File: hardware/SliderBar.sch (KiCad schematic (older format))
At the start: 36 parts, among them J1 USB_B_Mini, J2 MOTOR_OUT, J3 POT_IN, J4 DEBUG, U1 MIC5205-3.3YM5, U2 MT3608, U3 STM32F072C8Tx, U4 TB6612FNG

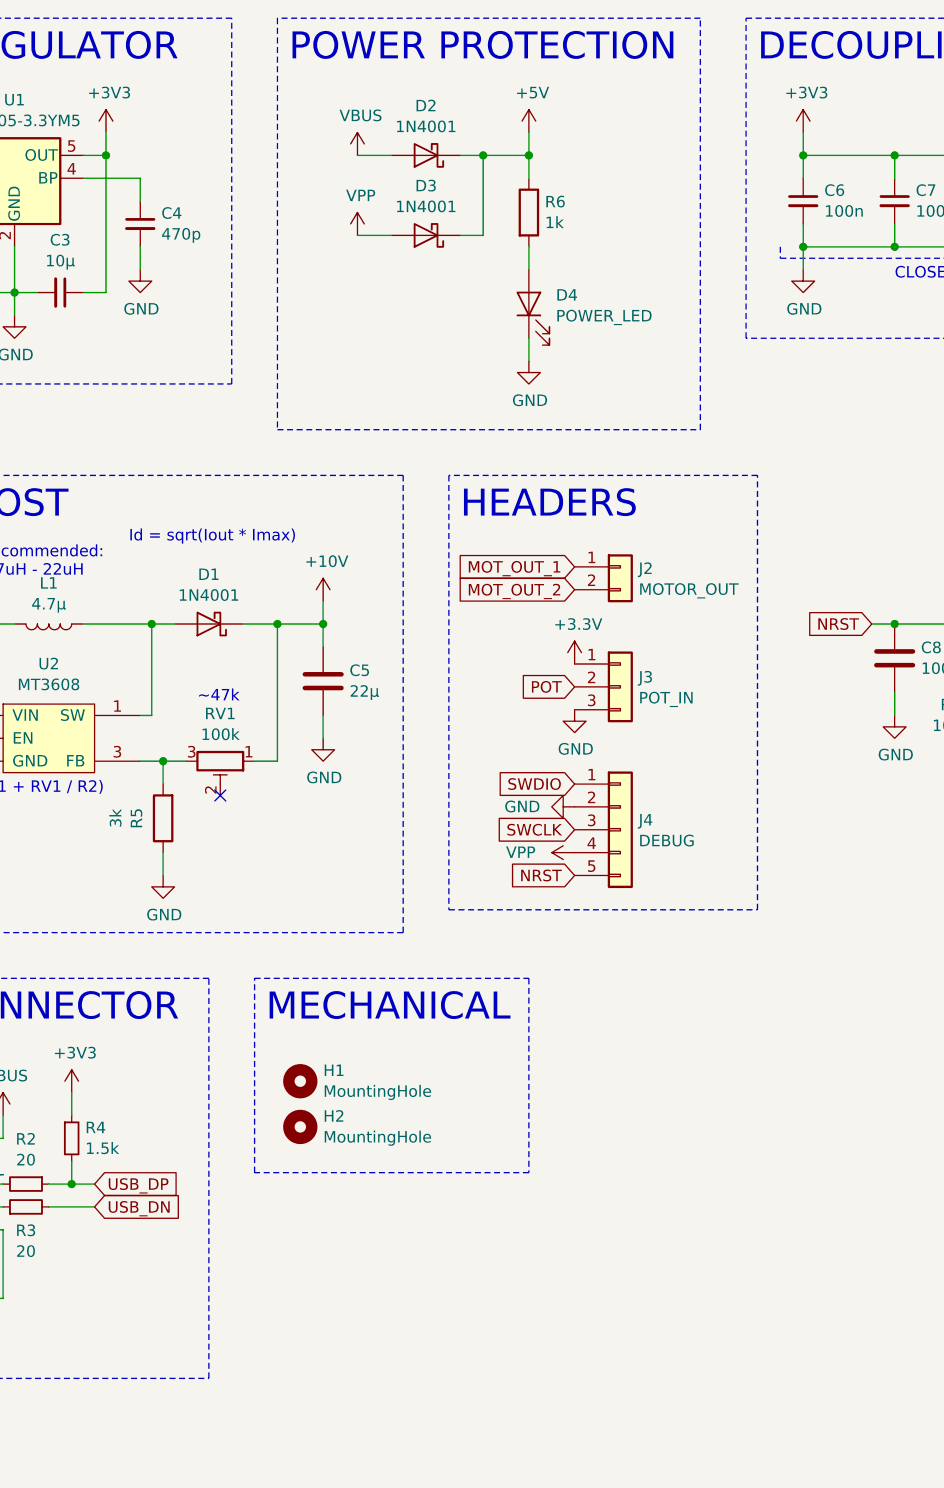
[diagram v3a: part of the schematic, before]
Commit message: Fix potentiometer wiring, move Nelib library outside of project
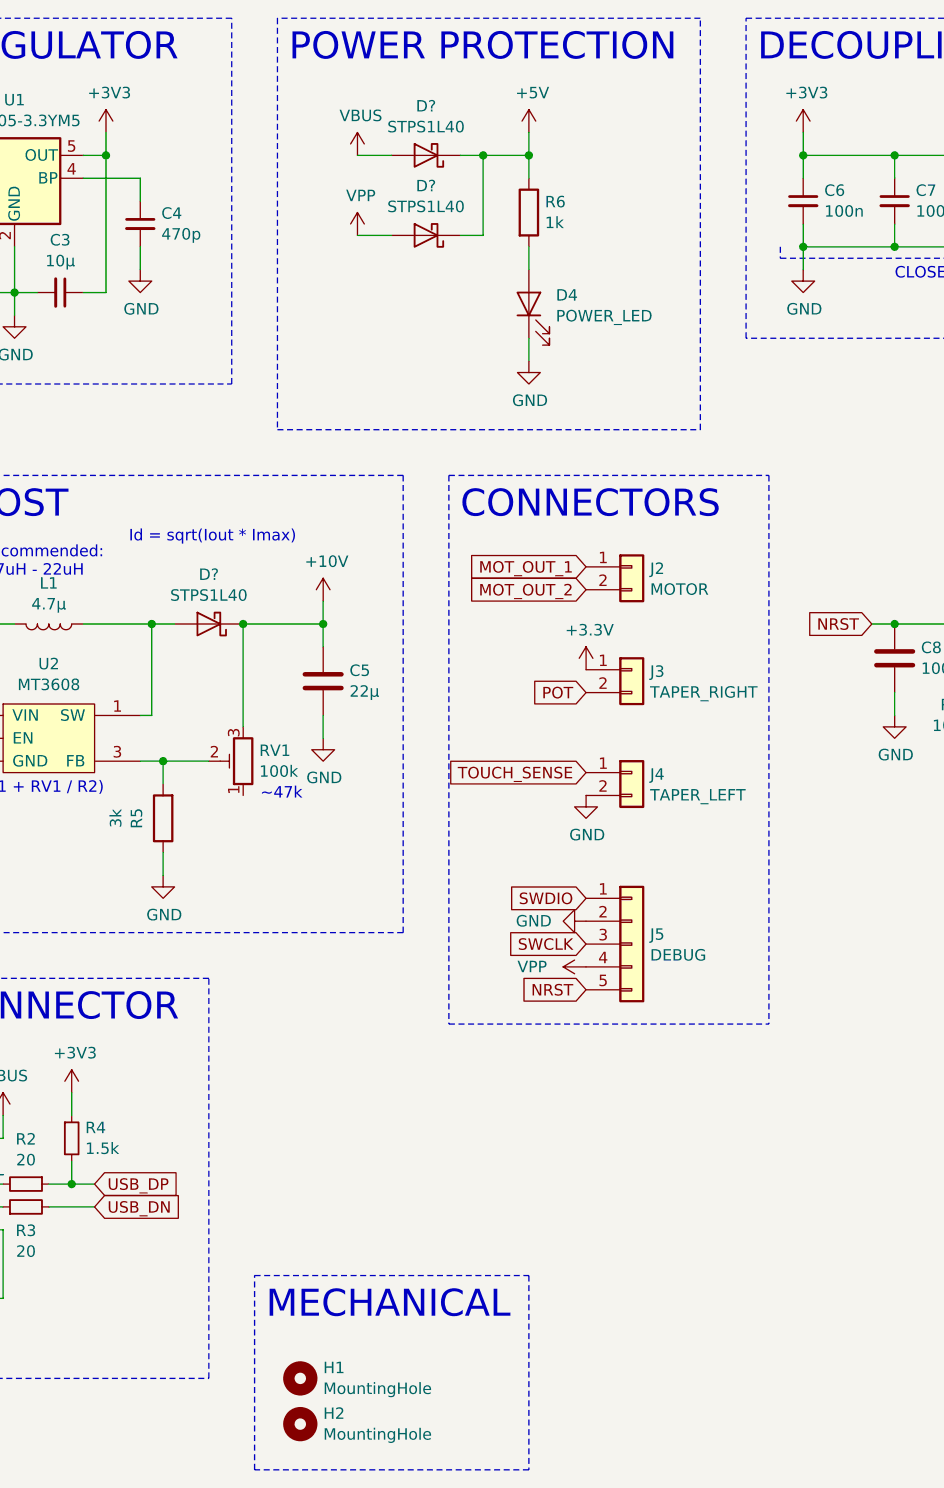
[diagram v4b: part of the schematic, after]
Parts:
- removed D1, D2, D3: 1N4001, Diode_SMD:D_SMA_Handsoldering, symbol Device:D_Schottky
- removed J3: POT_IN, Connector_Molex:Molex_PicoBlade_53048-0310_1x03_P1.25mm_Horizontal, symbol Connector_Generic:Conn_01x03
- added D? (x3): STPS1L40, Diode_SMD:D_SMA, symbol nelib:STPS1L40
- added J3: TAPER_RIGHT, Connector_Molex:Molex_PicoBlade_53048-0210_1x02_P1.25mm_Horizontal, symbol Connector_Generic:Conn_01x02
- added J4: TAPER_LEFT, Connector_Molex:Molex_PicoBlade_53048-0210_1x02_P1.25mm_Horizontal, symbol Connector_Generic:Conn_01x02
- C13: footprint Capacitor_Tantalum_SMD:CP_EIA-7343-15_Kemet-W -> Capacitor_Tantalum_SMD:CP_EIA-6032-28_Kemet-C_Pad2.25x2.35mm_HandSolder
- H1, H2: footprint MountingHole:MountingHole_3.2mm_M3_ISO14580 -> MountingHole:MountingHole_2.2mm_M2_Pad
- J2: value MOTOR_OUT -> MOTOR
- renumbered J4 to J5
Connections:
- net +10V: now also RV1.3, D?.1 (K); no longer RV1.1
- net +3V3: now also J3.1 (Pin_1)
- net +5V: now also D?.1 (K), D?.1 (K)
- net GND: now also J4.2 (Pin_2)
- net POT: now also J3.2 (Pin_2)
- net VBUS: now also D?.2 (A)
- net VPP: now also D?.2 (A)
- net at L1.1, U2.1 (SW): now also D?.2 (A)
- net at R5.2, U2.3 (FB): now also RV1.2; no longer RV1.3
- new net TOUCH_SENSE: J4.1 (Pin_1)
- no-connect marks 36 -> 35
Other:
- note added: "CONNECTORS"
- note removed: "HEADERS"
- moved on the sheet: H1, H2, J5, RV1

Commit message: Add touch sense connection
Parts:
- gave numbers to parts that had none: 3
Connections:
- net TOUCH_SENSE: now also U3.19 (PB1)
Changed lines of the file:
@@
 	5900 3350 5350 3350
 Connection ~ 5350 3350
-NoConn ~ 5900 4550
 NoConn ~ 5900 4650
 NoConn ~ 5900 4750
@@
 	3400 5100 4800 5100
 $Comp
-L nelib:STPS1L40 D?
+L nelib:STPS1L40 D2
 U 1 1 5C4BAB9A
 P 3300 1300
-F 0 "D?" H 3300 1085 50  0000 C CNN
+F 0 "D2" H 3300 1085 50  0000 C CNN
 F 1 "STPS1L40" H 3300 1176 50  0000 C CNN
 F 2 "Diode_SMD:D_SMA" H 3300 1125 50  0001 C CNN
@@
 $EndComp
 $Comp
-L nelib:STPS1L40 D?
+L nelib:STPS1L40 D3
 U 1 1 5C4C2FBE
 P 3300 1650
-F 0 "D?" H 3300 1434 50  0000 C CNN
+F 0 "D3" H 3300 1434 50  0000 C CNN
 F 1 "STPS1L40" H 3300 1525 50  0000 C CNN
 F 2 "Diode_SMD:D_SMA" H 3300 1475 50  0001 C CNN
@@
 $EndComp
 $Comp
-L nelib:STPS1L40 D?
+L nelib:STPS1L40 D1
 U 1 1 5C4C4325
 P 2350 3350
-F 0 "D?" H 2350 3134 50  0000 C CNN
+F 0 "D1" H 2350 3134 50  0000 C CNN
 F 1 "STPS1L40" H 2350 3225 50  0000 C CNN
 F 2 "Diode_SMD:D_SMA" H 2350 3175 50  0001 C CNN
@@
 Wire Wire Line
 	2150 3950 2350 3950
+NoConn ~ 2500 4100
+Text GLabel 5900 4550 0    50   Input ~ 0
+TOUCH_SENSE
 $EndSCHEMATC

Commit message: Fix capacitor valuee
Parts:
- C12: value 100nF -> 100n
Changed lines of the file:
@@
 P 10200 3550
 F 0 "C12" V 9971 3550 50  0000 C CNN
-F 1 "100nF" V 10062 3550 50  0000 C CNN
+F 1 "100n" V 10062 3550 50  0000 C CNN
 F 2 "Capacitor_SMD:C_1206_3216Metric_Pad1.42x1.75mm_HandSolder" H 10200 3550 50  0001 C CNN
 F 3 "~" H 10200 3550 50  0001 C CNN

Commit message: Add some 3D models from internet, fix some things
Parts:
- C1, C10, C11, C12, C2, C3, C4, C5, C6, C7, C8, C9: footprint Capacitor_SMD:C_1206_3216Metric_Pad1.42x1.75mm_HandSolder -> Capacitor_SMD:C_0805_2012Metric_Pad1.15x1.40mm_HandSolder
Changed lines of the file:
@@
 F 0 "C8" H 5465 3546 50  0000 L CNN
 F 1 "100n" H 5465 3455 50  0000 L CNN
-F 2 "Capacitor_SMD:C_1206_3216Metric_Pad1.42x1.75mm_HandSolder" H 5388 3350 50  0001 C CNN
+F 2 "Capacitor_SMD:C_0805_2012Metric_Pad1.15x1.40mm_HandSolder" H 5388 3350 50  0001 C CNN
 F 3 "~" H 5350 3500 50  0001 C CNN
 	1    5350 3500
@@
 F 0 "C4" H 2142 1646 50  0000 L CNN
 F 1 "470p" H 2142 1555 50  0000 L CNN
-F 2 "Capacitor_SMD:C_1206_3216Metric_Pad1.42x1.75mm_HandSolder" H 2050 1600 50  0001 C CNN
+F 2 "Capacitor_SMD:C_0805_2012Metric_Pad1.15x1.40mm_HandSolder" H 2050 1600 50  0001 C CNN
 F 3 "~" H 2050 1600 50  0001 C CNN
 	1    2050 1600
@@
 F 0 "C2" V 1071 1900 50  0000 C CNN
 F 1 "10µ" V 1162 1900 50  0000 C CNN
-F 2 "Capacitor_SMD:C_1206_3216Metric_Pad1.42x1.75mm_HandSolder" H 1300 1900 50  0001 C CNN
+F 2 "Capacitor_SMD:C_0805_2012Metric_Pad1.15x1.40mm_HandSolder" H 1300 1900 50  0001 C CNN
 F 3 "~" H 1300 1900 50  0001 C CNN
 	1    1300 1900
@@
 F 0 "C3" V 1471 1900 50  0000 C CNN
 F 1 "10µ" V 1562 1900 50  0000 C CNN
-F 2 "Capacitor_SMD:C_1206_3216Metric_Pad1.42x1.75mm_HandSolder" H 1700 1900 50  0001 C CNN
+F 2 "Capacitor_SMD:C_0805_2012Metric_Pad1.15x1.40mm_HandSolder" H 1700 1900 50  0001 C CNN
 F 3 "~" H 1700 1900 50  0001 C CNN
 	1    1700 1900
@@
 F 0 "C5" H 2735 3554 50  0000 R CNN
 F 1 "22µ" H 2735 3645 50  0000 R CNN
-F 2 "Capacitor_SMD:C_1206_3216Metric_Pad1.42x1.75mm_HandSolder" H 2888 3450 50  0001 C CNN
+F 2 "Capacitor_SMD:C_0805_2012Metric_Pad1.15x1.40mm_HandSolder" H 2888 3450 50  0001 C CNN
 F 3 "~" H 2850 3600 50  0001 C CNN
 	1    2850 3600
@@
 F 0 "C1" H 1015 3646 50  0000 L CNN
 F 1 "22µ" H 1015 3555 50  0000 L CNN
-F 2 "Capacitor_SMD:C_1206_3216Metric_Pad1.42x1.75mm_HandSolder" H 938 3450 50  0001 C CNN
+F 2 "Capacitor_SMD:C_0805_2012Metric_Pad1.15x1.40mm_HandSolder" H 938 3450 50  0001 C CNN
 F 3 "~" H 900 3600 50  0001 C CNN
 	1    900  3600
@@
 F 0 "C12" V 9971 3550 50  0000 C CNN
 F 1 "100n" V 10062 3550 50  0000 C CNN
-F 2 "Capacitor_SMD:C_1206_3216Metric_Pad1.42x1.75mm_HandSolder" H 10200 3550 50  0001 C CNN
+F 2 "Capacitor_SMD:C_0805_2012Metric_Pad1.15x1.40mm_HandSolder" H 10200 3550 50  0001 C CNN
 F 3 "~" H 10200 3550 50  0001 C CNN
 	1    10200 3550
@@
 F 0 "C6" H 5042 1546 50  0000 L CNN
 F 1 "100n" H 5042 1455 50  0000 L CNN
-F 2 "Capacitor_SMD:C_1206_3216Metric_Pad1.42x1.75mm_HandSolder" H 4950 1500 50  0001 C CNN
+F 2 "Capacitor_SMD:C_0805_2012Metric_Pad1.15x1.40mm_HandSolder" H 4950 1500 50  0001 C CNN
 F 3 "~" H 4950 1500 50  0001 C CNN
 	1    4950 1500
@@
 F 0 "C7" H 5442 1546 50  0000 L CNN
 F 1 "100n" H 5442 1455 50  0000 L CNN
-F 2 "Capacitor_SMD:C_1206_3216Metric_Pad1.42x1.75mm_HandSolder" H 5350 1500 50  0001 C CNN
+F 2 "Capacitor_SMD:C_0805_2012Metric_Pad1.15x1.40mm_HandSolder" H 5350 1500 50  0001 C CNN
 F 3 "~" H 5350 1500 50  0001 C CNN
 	1    5350 1500
@@
 F 0 "C9" H 5842 1546 50  0000 L CNN
 F 1 "100n" H 5842 1455 50  0000 L CNN
-F 2 "Capacitor_SMD:C_1206_3216Metric_Pad1.42x1.75mm_HandSolder" H 5750 1500 50  0001 C CNN
+F 2 "Capacitor_SMD:C_0805_2012Metric_Pad1.15x1.40mm_HandSolder" H 5750 1500 50  0001 C CNN
 F 3 "~" H 5750 1500 50  0001 C CNN
 	1    5750 1500
@@
 F 0 "C10" H 6242 1546 50  0000 L CNN
 F 1 "4.7µ" H 6242 1455 50  0000 L CNN
-F 2 "Capacitor_SMD:C_1206_3216Metric_Pad1.42x1.75mm_HandSolder" H 6150 1500 50  0001 C CNN
+F 2 "Capacitor_SMD:C_0805_2012Metric_Pad1.15x1.40mm_HandSolder" H 6150 1500 50  0001 C CNN
 F 3 "~" H 6150 1500 50  0001 C CNN
 	1    6150 1500
@@
 F 0 "C11" H 6792 1546 50  0000 L CNN
 F 1 "100n" H 6792 1455 50  0000 L CNN
-F 2 "Capacitor_SMD:C_1206_3216Metric_Pad1.42x1.75mm_HandSolder" H 6700 1500 50  0001 C CNN
+F 2 "Capacitor_SMD:C_0805_2012Metric_Pad1.15x1.40mm_HandSolder" H 6700 1500 50  0001 C CNN
 F 3 "~" H 6700 1500 50  0001 C CNN
 	1    6700 1500

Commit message: Removed USB DP/DM resistors & Placed connectors
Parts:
- removed R2, R3: 20, Resistor_SMD:R_1206_3216Metric_Pad1.42x1.75mm_HandSolder, symbol Device:R_Small
- J2, J3, J4: footprint Connector_Molex:Molex_PicoBlade_53048-0210_1x02_P1.25mm_Horizontal -> Connector_JST:JST_GH_SM02B-GHS-TB_1x02-1MP_P1.25mm_Horizontal
- J5: footprint Connector_Molex:Molex_PicoBlade_53047-0510_1x05_P1.25mm_Vertical -> Connector_JST:JST_GH_BM05B-GHS-TBT_1x05-1MP_P1.25mm_Vertical
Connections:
- net D+ is gone; now on net USB_DP: J1.3 (D+)
- net D- is gone; now on net USB_DN: J1.2 (D-)
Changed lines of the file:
@@
 F 0 "J5" H 4280 4792 50  0000 L CNN
 F 1 "DEBUG" H 4280 4701 50  0000 L CNN
-F 2 "Connector_Molex:Molex_PicoBlade_53047-0510_1x05_P1.25mm_Vertical" H 4200 4750 50  0001 C CNN
+F 2 "Connector_JST:JST_GH_BM05B-GHS-TBT_1x05-1MP_P1.25mm_Vertical" H 4200 4750 50  0001 C CNN
 F 3 "~" H 4200 4750 50  0001 C CNN
 	1    4200 4750
@@
 USB_DP
 $Comp
-L Device:R_Small R2
-U 1 1 5BDCCEB2
-P 1550 5800
-F 0 "R2" V 1354 5800 50  0000 C CNN
-F 1 "20" V 1445 5800 50  0000 C CNN
-F 2 "Resistor_SMD:R_1206_3216Metric_Pad1.42x1.75mm_HandSolder" H 1550 5800 50  0001 C CNN
-F 3 "~" H 1550 5800 50  0001 C CNN
-	1    1550 5800
-	0    1    1    0
-$EndComp
-$Comp
-L Device:R_Small R3
-U 1 1 5BDCCFBC
-P 1550 5900
-F 0 "R3" V 1446 5900 50  0000 C CNN
-F 1 "20" V 1355 5900 50  0000 C CNN
-F 2 "Resistor_SMD:R_1206_3216Metric_Pad1.42x1.75mm_HandSolder" H 1550 5900 50  0001 C CNN
-F 3 "~" H 1550 5900 50  0001 C CNN
-	1    1550 5900
-	0    -1   -1   0
-$EndComp
-$Comp
 L Device:R_Small R4
 U 1 1 5BDD3A19
@@
 Wire Wire Line
 	1750 5400 1750 5500
-Wire Wire Line
-	1650 5800 1750 5800
-Wire Wire Line
-	1850 5900 1650 5900
-Wire Wire Line
-	1450 5900 1350 5900
-Wire Wire Line
-	1350 5800 1450 5800
 Wire Wire Line
 	1750 5700 1750 5800
@@
 F 0 "J3" H 4280 3542 50  0000 L CNN
 F 1 "TAPER_RIGHT" H 4280 3451 50  0000 L CNN
-F 2 "Connector_Molex:Molex_PicoBlade_53048-0210_1x02_P1.25mm_Horizontal" H 4200 3550 50  0001 C CNN
+F 2 "Connector_JST:JST_GH_SM02B-GHS-TB_1x02-1MP_P1.25mm_Horizontal" H 4200 3550 50  0001 C CNN
 F 3 "~" H 4200 3550 50  0001 C CNN
 	1    4200 3550
@@
 F 0 "J4" H 4280 3992 50  0000 L CNN
 F 1 "TAPER_LEFT" H 4280 3901 50  0000 L CNN
-F 2 "Connector_Molex:Molex_PicoBlade_53048-0210_1x02_P1.25mm_Horizontal" H 4200 4000 50  0001 C CNN
+F 2 "Connector_JST:JST_GH_SM02B-GHS-TB_1x02-1MP_P1.25mm_Horizontal" H 4200 4000 50  0001 C CNN
 F 3 "~" H 4200 4000 50  0001 C CNN
 	1    4200 4000
@@
 F 0 "J2" H 4280 3092 50  0000 L CNN
 F 1 "MOTOR" H 4280 3001 50  0000 L CNN
-F 2 "Connector_Molex:Molex_PicoBlade_53048-0210_1x02_P1.25mm_Horizontal" H 4200 3100 50  0001 C CNN
+F 2 "Connector_JST:JST_GH_SM02B-GHS-TB_1x02-1MP_P1.25mm_Horizontal" H 4200 3100 50  0001 C CNN
 F 3 "~" H 4200 3100 50  0001 C CNN
 	1    4200 3100
@@
 Text GLabel 5900 4550 0    50   Input ~ 0
 TOUCH_SENSE
+Wire Wire Line
+	1350 5800 1750 5800
+Wire Wire Line
+	1350 5900 1850 5900
 $EndSCHEMATC
